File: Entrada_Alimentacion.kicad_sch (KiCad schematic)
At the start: 5 parts, among them J3 +12V2, J4 +3V3, J5 +/- 5V, J6 +/- 12V, J7 INPUT_CEDCp

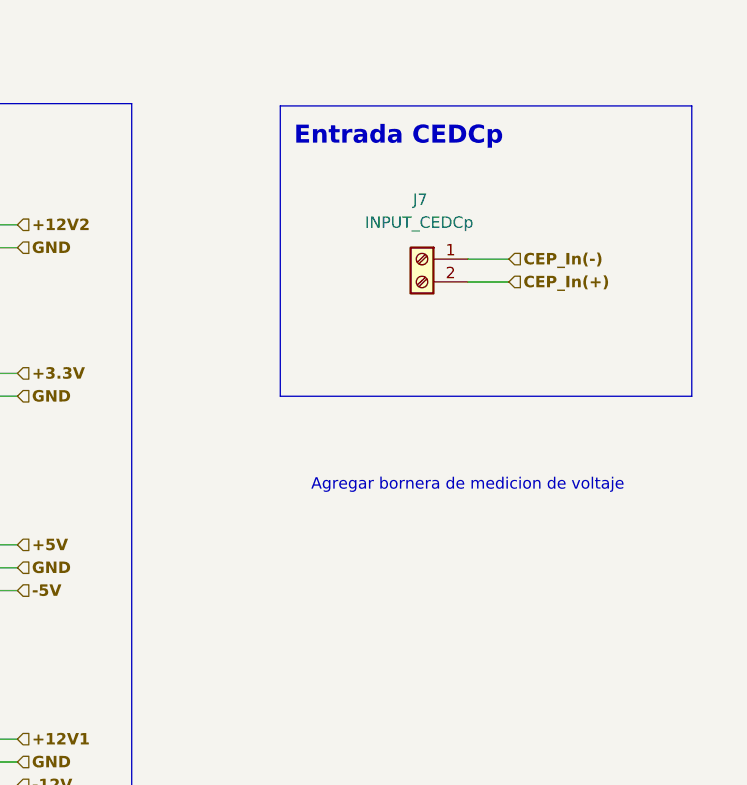
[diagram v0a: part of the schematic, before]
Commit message: Reorder conection with control module
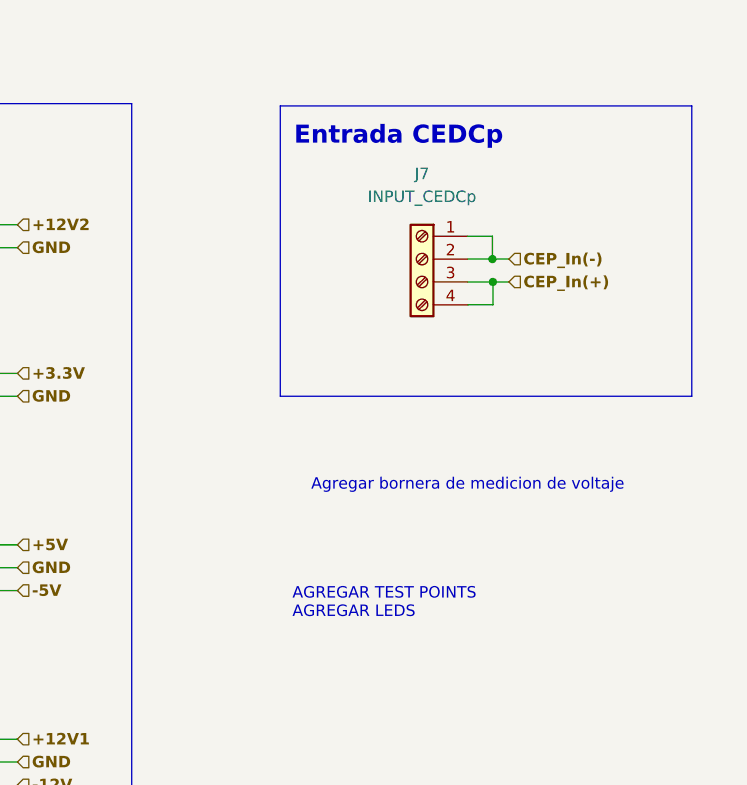
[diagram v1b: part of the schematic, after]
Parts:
- removed J7: INPUT_CEDCp, CEDCp:Bornera_1x2, symbol Connector:Screw_Terminal_01x02
- added J7: INPUT_CEDCp, CEDCp:Bornera_1x4, symbol Connector:Screw_Terminal_01x04
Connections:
- net CEP_In(+): now also J7.3 (Pin_3), J7.4 (Pin_4)
- net CEP_In(-): now also J7.1 (Pin_1), J7.2 (Pin_2)
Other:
- note added: "AGREGAR TEST POINTS AGREGAR LEDS"
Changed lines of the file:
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@@
 (kicad_sch (version 20211123) (generator eeschema)
   (paper "A4")
-  (wire (pts (xy 180.848 77.47) (xy 185.42 77.47))
+  (junction (at 183.642 77.47) (diameter 0) (color 0 0 0 0)
+  )
+  (junction (at 183.5912 74.93) (diameter 0) (color 0 0 0 0)
+  )
+  (wire (pts (xy 180.848 77.47) (xy 183.642 77.47))
     (stroke (width 0) (type default) (color 0 0 0 0))
   )
@@
     (stroke (width 0) (type default) (color 0 0 0 0))
   )
+  (wire (pts (xy 180.848 80.01) (xy 183.642 80.01))
+    (stroke (width 0) (type default) (color 0 0 0 0))
+  )
   (polyline (pts (xy 205.74 57.912) (xy 205.74 90.17))
     (stroke (width 0) (type default) (color 0 0 0 0))
@@
     (stroke (width 0) (type default) (color 0 0 0 0))
   )
+  (wire (pts (xy 180.848 72.39) (xy 183.5912 72.39))
+    (stroke (width 0) (type default) (color 0 0 0 0))
+  )
   (polyline (pts (xy 205.74 90.17) (xy 160.02 90.17))
     (stroke (width 0) (type default) (color 0 0 0 0))
@@
     (stroke (width 0) (type default) (color 0 0 0 0))
   )
-  (wire (pts (xy 180.848 74.93) (xy 185.42 74.93))
+  (wire (pts (xy 183.5912 74.93) (xy 185.42 74.93))
+    (stroke (width 0) (type default) (color 0 0 0 0))
+  )
+  (wire (pts (xy 183.642 80.01) (xy 183.642 77.47))
+    (stroke (width 0) (type default) (color 0 0 0 0))
+  )
+  (wire (pts (xy 183.642 77.47) (xy 185.42 77.47))
+    (stroke (width 0) (type default) (color 0 0 0 0))
+  )
+  (wire (pts (xy 180.848 74.93) (xy 183.5912 74.93))
     (stroke (width 0) (type default) (color 0 0 0 0))
   )
@@
   )
   (wire (pts (xy 118.11 87.63) (xy 130.81 87.63))
+    (stroke (width 0) (type default) (color 0 0 0 0))
+  )
+  (wire (pts (xy 183.5912 72.39) (xy 183.5912 74.93))
     (stroke (width 0) (type default) (color 0 0 0 0))
   )
@@
   (text "Entrada CEDCp\n" (at 161.544 62.484 0)
     (effects (font (size 2 2) bold) (justify left bottom))
+  )
+  (text "AGREGAR TEST POINTS\nAGREGAR LEDS " (at 161.3662 114.9858 0)
+    (effects (font (size 1.27 1.27)) (justify left bottom))
   )
   (label "+12V1" (at 120.65 128.27 0)
@@
       (effects (font (size 1.27 1.27)) hide)
     )
-    (property "Datasheet" "~" (id 3) (at 113.03 87.63 0)
+    (property "Datasheet" "https://www.degson.com/content/details_552_880840.html?lang=en" (id 3) (at 113.03 87.63 0)
       (effects (font (size 1.27 1.27)) hide)
     )
@@
     (pin "3")
   )
-  (symbol (lib_id "Connector:Screw_Terminal_01x02") (at 175.768 74.93 0) (mirror y) (unit 1)
-    (in_bom yes) (on_board yes)
-    (property "Reference" "J7" (id 0) (at 174.752 68.326 0)
-      (effects (font (size 1.27 1.27)) (justify right))
-    )
-    (property "Value" "INPUT_CEDCp" (id 1) (at 169.418 70.866 0)
-      (effects (font (size 1.27 1.27)) (justify right))
-    )
-    (property "Footprint" "CEDCp:Bornera_1x2" (id 2) (at 175.768 74.93 0)
-      (effects (font (size 1.27 1.27)) hide)
-    )
-    (property "Datasheet" "https://www.degson.com/content/details_552_880840.html?lang=en" (id 3) (at 175.768 74.93 0)
-      (effects (font (size 1.27 1.27)) hide)
-    )
-    (pin "1")
-    (pin "2")
+  (symbol (lib_id "Connector:Screw_Terminal_01x04") (at 175.768 74.93 0) (mirror y) (unit 1)
+    (in_bom yes) (on_board yes) (fields_autoplaced)
+    (property "Reference" "J7" (id 0) (at 175.768 65.4558 0))
+    (property "Value" "INPUT_CEDCp" (id 1) (at 175.768 67.9958 0))
+    (property "Footprint" "CEDCp:Bornera_1x4" (id 2) (at 175.768 74.93 0)
+      (effects (font (size 1.27 1.27)) hide)
+    )
+    (property "Datasheet" "https://www.degson.com/content/details_552_880838.html?lang=en" (id 3) (at 175.768 74.93 0)
+      (effects (font (size 1.27 1.27)) hide)
+    )
+    (pin "1")
+    (pin "2")
+    (pin "3")
+    (pin "4")
   )
   (symbol (lib_id "Connector:Screw_Terminal_01x02") (at 113.03 71.12 0) (mirror y) (unit 1)

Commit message: Gerbers generated again
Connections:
- net CEP_In(+) renamed CEP_Inpunt+_1
- net CEP_Inpunt+_1: no longer J7.3 (Pin_3)
- new net CEP_Inpunt+_2: J7.3 (Pin_3)
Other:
- moved on the sheet: J7
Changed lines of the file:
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@@
 (kicad_sch (version 20211123) (generator eeschema)
   (paper "A4")
-  (junction (at 183.642 77.47) (diameter 0) (color 0 0 0 0)
-  )
-  (junction (at 183.5912 74.93) (diameter 0) (color 0 0 0 0)
-  )
-  (wire (pts (xy 180.848 77.47) (xy 183.642 77.47))
-    (stroke (width 0) (type default) (color 0 0 0 0))
+  (junction (at 183.134 77.8256) (diameter 0) (color 0 0 0 0)
   )
   (polyline (pts (xy 96.52 142.24) (xy 96.52 57.658))
     (stroke (width 0) (type default) (color 0 0 0 0))
   )
-  (wire (pts (xy 180.848 80.01) (xy 183.642 80.01))
+  (wire (pts (xy 183.134 77.8256) (xy 185.42 77.8256))
     (stroke (width 0) (type default) (color 0 0 0 0))
   )
@@
     (stroke (width 0) (type default) (color 0 0 0 0))
   )
+  (wire (pts (xy 183.134 80.3656) (xy 183.134 77.8256))
+    (stroke (width 0) (type default) (color 0 0 0 0))
+  )
   (polyline (pts (xy 143.51 57.658) (xy 143.51 142.24))
     (stroke (width 0) (type default) (color 0 0 0 0))
@@
     (stroke (width 0) (type default) (color 0 0 0 0))
   )
-  (wire (pts (xy 180.848 72.39) (xy 183.5912 72.39))
-    (stroke (width 0) (type default) (color 0 0 0 0))
-  )
   (polyline (pts (xy 205.74 90.17) (xy 160.02 90.17))
     (stroke (width 0) (type default) (color 0 0 0 0))
@@
     (stroke (width 0) (type default) (color 0 0 0 0))
   )
+  (wire (pts (xy 180.6702 72.7456) (xy 185.42 72.7456))
+    (stroke (width 0) (type default) (color 0 0 0 0))
+  )
   (polyline (pts (xy 160.02 57.912) (xy 205.74 57.912))
     (stroke (width 0) (type default) (color 0 0 0 0))
@@
     (stroke (width 0) (type default) (color 0 0 0 0))
   )
-  (wire (pts (xy 183.5912 74.93) (xy 185.42 74.93))
-    (stroke (width 0) (type default) (color 0 0 0 0))
-  )
-  (wire (pts (xy 183.642 80.01) (xy 183.642 77.47))
-    (stroke (width 0) (type default) (color 0 0 0 0))
-  )
-  (wire (pts (xy 183.642 77.47) (xy 185.42 77.47))
-    (stroke (width 0) (type default) (color 0 0 0 0))
-  )
-  (wire (pts (xy 180.848 74.93) (xy 183.5912 74.93))
-    (stroke (width 0) (type default) (color 0 0 0 0))
-  )
   (wire (pts (xy 118.11 133.35) (xy 130.81 133.35))
     (stroke (width 0) (type default) (color 0 0 0 0))
@@
     (stroke (width 0) (type default) (color 0 0 0 0))
   )
+  (wire (pts (xy 180.6702 80.3656) (xy 183.134 80.3656))
+    (stroke (width 0) (type default) (color 0 0 0 0))
+  )
   (polyline (pts (xy 160.02 57.912) (xy 160.02 90.17))
     (stroke (width 0) (type default) (color 0 0 0 0))
@@
     (stroke (width 0) (type default) (color 0 0 0 0))
   )
-  (wire (pts (xy 183.5912 72.39) (xy 183.5912 74.93))
+  (wire (pts (xy 180.6702 75.2856) (xy 185.42 75.2856))
     (stroke (width 0) (type default) (color 0 0 0 0))
   )
   (wire (pts (xy 118.11 90.17) (xy 130.81 90.17))
+    (stroke (width 0) (type default) (color 0 0 0 0))
+  )
+  (wire (pts (xy 180.6702 77.8256) (xy 183.134 77.8256))
     (stroke (width 0) (type default) (color 0 0 0 0))
   )
@@
     (effects (font (size 1.27 1.27) (thickness 0.254) bold) (justify left))
   )
-  (hierarchical_label "CEP_In(-)" (shape input) (at 185.42 74.93 0)
+  (hierarchical_label "CEP_Inpunt+_2" (shape input) (at 185.42 75.2856 0)
+    (effects (font (size 1.27 1.27) (thickness 0.254) bold) (justify left))
+  )
+  (hierarchical_label "CEP_In(-)" (shape input) (at 185.42 77.8256 0)
     (effects (font (size 1.27 1.27) (thickness 0.254) bold) (justify left))
   )
@@
     (effects (font (size 1.27 1.27) (thickness 0.254) bold) (justify left))
   )
-  (hierarchical_label "CEP_In(+)" (shape input) (at 185.42 77.47 0)
+  (hierarchical_label "CEP_Inpunt+_1" (shape input) (at 185.42 72.7456 0)
     (effects (font (size 1.27 1.27) (thickness 0.254) bold) (justify left))
   )
@@
     (pin "3")
   )
-  (symbol (lib_id "Connector:Screw_Terminal_01x04") (at 175.768 74.93 0) (mirror y) (unit 1)
+  (symbol (lib_id "Connector:Screw_Terminal_01x04") (at 175.5902 77.8256 180) (unit 1)
     (in_bom yes) (on_board yes) (fields_autoplaced)
-    (property "Reference" "J7" (id 0) (at 175.768 65.4558 0))
-    (property "Value" "INPUT_CEDCp" (id 1) (at 175.768 67.9958 0))
-    (property "Footprint" "CEDCp:Bornera_1x4" (id 2) (at 175.768 74.93 0)
-      (effects (font (size 1.27 1.27)) hide)
-    )
-    (property "Datasheet" "https://www.degson.com/content/details_552_880838.html?lang=en" (id 3) (at 175.768 74.93 0)
-      (effects (font (size 1.27 1.27)) hide)
-    )
+    (property "Reference" "J7" (id 0) (at 175.5902 66.3956 0))
+    (property "Value" "INPUT_CEDCp" (id 1) (at 175.5902 68.9356 0))
+    (property "Footprint" "CEDCp:Bornera_1x4" (id 2) (at 175.5902 77.8256 0)
+      (effects (font (size 1.27 1.27)) hide)
+    )
+    (property "Datasheet" "https://www.degson.com/content/details_552_880838.html?lang=en" (id 3) (at 175.5902 77.8256 0)
+      (effects (font (size 1.27 1.27)) hide)
+    )

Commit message: V4 Ltspice
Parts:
- removed J7: INPUT_CEDCp, CEDCp:Bornera_1x4, symbol Connector:Screw_Terminal_01x04
- added J11, J13: Conn_01x01, Connector_Wire:SolderWire-2sqmm_1x01_D2mm_OD3.9mm, symbol Connector_Generic:Conn_01x01
- added J12, J14: Conn_01x01, Connector_Wire:SolderWire-0.5sqmm_1x01_D0.9mm_OD2.3mm, symbol Connector_Generic:Conn_01x01
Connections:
- net +12V2: now also J3.2 (Pin_2); no longer J3.1 (Pin_1)
- net +5V: now also J5.3 (Pin_3); no longer J5.1 (Pin_1)
- net -5V: now also J5.1 (Pin_1); no longer J5.3 (Pin_3)
- net CEP_In(-): now also J13.1 (Pin_1), J14.1 (Pin_1)
- net CEP_Inpunt+_1: now also J11.1 (Pin_1)
- net CEP_Inpunt+_2: now also J12.1 (Pin_1)
- net GND: now also J3.1 (Pin_1); no longer J3.2 (Pin_2)
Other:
- moved on the sheet: J3
